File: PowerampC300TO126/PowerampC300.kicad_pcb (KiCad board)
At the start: 2 copper layers, 240 x 63 mm, 110 parts, among them J1 Conn_01x02, J2 Conn_01x02, J3 Conn_01x02, J4 Conn_01x01, J5 Conn_01x01, J6 Conn_01x01, J7 Conn_01x01, J8 Conn_01x02, J9 Conn_Coaxial, Q1 2N5551, Q10 MJE350, Q11 MJE340, Q12 MJE340, Q13 2N5551, Q14 2N5401, Q15 MJE340, Q16 MJE350, Q17 MJL3281A, Q18 MJL1302A, Q19 MJL3281A, Q2 2N5551, Q20 MJL1302A, Q21 MJL3281A, Q22 MJL1302A, Q23 MJL3281A, Q24 MJL1302A, Q3 2N5401, Q4 2N5401, Q5 2N5551, Q6 2N5551, Q7 2N5551, Q8 2N5401

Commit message: Added instructions
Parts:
- moved R24 21.3 mm to (186.4, 75.5)
- moved C5 13.8 mm to (196.5, 73.7), turned to 180 degrees
- moved R12 13.5 mm to (189.0, 69.0)
- moved C22 11.8 mm to (192.8, 69.0), turned to 0 degrees
- moved R28 11.5 mm to (182.1, 69.2)
- moved Q14 10.4 mm to (163.3, 68.8)
- moved R4 6.80 mm to (89.2, 76.0)
- moved Q4 6.50 mm to (84.8, 85.2), turned to 0 degrees
- moved C13 6.31 mm to (84.4, 68.8)
- moved R27 6.30 mm to (178.8, 72.5), turned to 0 degrees
- moved Q3 5.40 mm to (99.7, 85.0), turned to 180 degrees
- moved Q7 5.33 mm to (186.3, 85.5), turned to 180 degrees
- moved Q10 2.85 mm to (119.5, 80.4)
- moved R17 2.50 mm to (101.0, 76.0)
- moved R3 2.20 mm to (97.6, 76.0)
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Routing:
- net -48V: track 300.6 -> 283.6 mm
- net Net-(D4-Pad2): track 19.2 -> 4.69 mm
- net Net-(C22-Pad1): track 45.4 -> 56.6 mm
- net Net-(C3-Pad2): track 41.2 -> 31.4 mm
- net Net-(Q14-Pad2): track 24.5 -> 34.3 mm
- net Net-(Q12-Pad1): track 10.4 -> 19.5 mm
- net Net-(Q11-Pad3): track 15.7 -> 21.9 mm
- net Net-(Q7-Pad3): track 5.07 -> 11.2 mm
- net Net-(D3-Pad1): track 9.05 -> 2.90 mm
- net Net-(Q3-Pad1): track 4.50 -> 10.1 mm
- net Net-(C6-Pad2): track 519.5 -> 524.4 mm
- net Net-(Q7-Pad1): track 5.19 -> 10.00 mm
- net Net-(Q13-Pad2): track 15.5 -> 20.0 mm
- net Net-(Q10-Pad3): track 50.8 -> 53.6 mm
- net Net-(C9-Pad1): track 25.4 -> 27.5 mm
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
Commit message: Added option for spade terminal power connections
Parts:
- J1, J2, J3: footprint Connectors_Terminal_Blocks:TerminalBlock_bornier-2_P5.08mm -> poweramp:TerminalBlock_bornier-2_P5.08mm_with_spade
- moved J1 5.87 mm to (226.0, 98.0)
- moved C11 2.20 mm to (232.0, 91.0)
- moved R43 1.48 mm to (194.0, 103.0)
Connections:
- J2 pad 1: -48V -> GND
- J2 pad 2: GND -> -48V
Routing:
- net -48V: track 283.6 -> 296.5 mm
- net GND: track 52.5 -> 57.5 mm
- net OUTPUT: track 28.8 -> 33.0 mm
- net Net-(C11-Pad2): track 3.54 -> 5.92 mm
- net +48V: track 307.4 -> 309.7 mm
- net Net-(C6-Pad2): track 524.4 -> 525.9 mm

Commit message: Added OITPC compensation
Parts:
- added C20: NC, Capacitors_THT:C_Disc_D5.0mm_W2.5mm_P5.00mm, F.Cu at (103.3, 90.4)
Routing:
- net Net-(C20-Pad1): track 27.5 -> 30.9 mm
- net Net-(C20-Pad2): track 525.9 -> 529.2 mm
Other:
- board text added: "MODIFIED C300 AMPLIFIER BY DANIEL MARKS CC-BY-SA 4.0 V3"
- board text removed: "MODIFIED C300 AMPLIFIER BY DANIEL MARKS ORIGINAL BY MICHAEL CHUA (AMPSLAB) CC-BY-SA 4.0 V2"

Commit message: Redid star scheme again, added grounding diagram, modified drill template
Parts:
- added D11: 1N4148, Diodes_THT:D_DO-35_SOD27_P7.62mm_Horizontal, F.Cu at (195.8, 104.0)
- added D12: 1N4148, Diodes_THT:D_DO-35_SOD27_P7.62mm_Horizontal, F.Cu at (203.4, 101.4)
- added R20: 10R, Resistors_THT:R_Axial_DIN0207_L6.3mm_D2.5mm_P7.62mm_Horizontal, F.Cu at (196.0, 98.8)
- moved C6 36.6 mm to (110.6, 104.6)
- moved C23 32.4 mm to (97.3, 101.8)
- moved C3 27.1 mm to (70.0, 105.0), turned to 90 degrees
- moved C8 27.0 mm to (99.0, 88.0)
- moved C13 25.6 mm to (110.0, 69.0), turned to 0 degrees
- moved R15 25.0 mm to (104.0, 97.0)
- moved R14 24.6 mm to (107.4, 97.0)
- moved R43 23.5 mm to (216.4, 95.8), turned to 180 degrees
- moved R18 22.7 mm to (133.0, 88.0)
- moved Q8 20.9 mm to (90.3, 86.5), turned to 270 degrees
- moved R5 20.7 mm to (79.7, 95.2), turned to 270 degrees
- moved C25 19.7 mm to (133.6, 73.3), turned to 180 degrees
- moved C24 19.5 mm to (141.0, 91.0), turned to 180 degrees
- moved R3 19.4 mm to (78.2, 76.1)
- moved R17 19.3 mm to (81.8, 76.1)
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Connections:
- C2 pad 1: GND -> GNDS
- C23 pad 1: GND -> GNDS
- C24 pad 2: GND -> GNDS
- C4 pad 1: GND -> GNDS
- C8 pad 1: GND -> GNDS
- D1 pad 2: GND -> GNDS
- J8 pad 2: GND -> GNDS
- J9 pad 2: GND -> GNDS
- JP2 pad 1: GND -> GNDS
- Q8 pad 3: GND -> GNDS
- R16 pad 2: GND -> GNDS
- R2 pad 2: GND -> GNDS
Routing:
- net Net-(C20-Pad2): track 529.2 -> 489.7 mm, vias 2 -> 0
- net GNDS: track 0.00 -> 37.6 mm
- net Net-(C6-Pad1): track 48.5 -> 16.7 mm
- net Net-(Q2-Pad3): track 26.8 -> 50.9 mm
- net Net-(C20-Pad1): track 30.9 -> 53.7 mm
- net Net-(Q1-Pad3): track 29.3 -> 47.7 mm
- net Net-(C25-Pad1): track 30.0 -> 45.1 mm
- net Net-(Q10-Pad3): track 53.6 -> 66.7 mm
- net Net-(C1-Pad1): track 19.9 -> 10.5 mm
- net Net-(C10-Pad1): track 70.7 -> 61.7 mm
- net Net-(Q10-Pad1): track 14.7 -> 23.4 mm
- net Net-(C3-Pad1): track 3.72 -> 11.1 mm
- net INPUT: track 27.9 -> 21.0 mm
- net +48V: track 309.7 -> 316.0 mm
- net Net-(Q15-Pad1): track 153.6 -> 159.6 mm
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- added copper zone on F.Cu, net GNDS

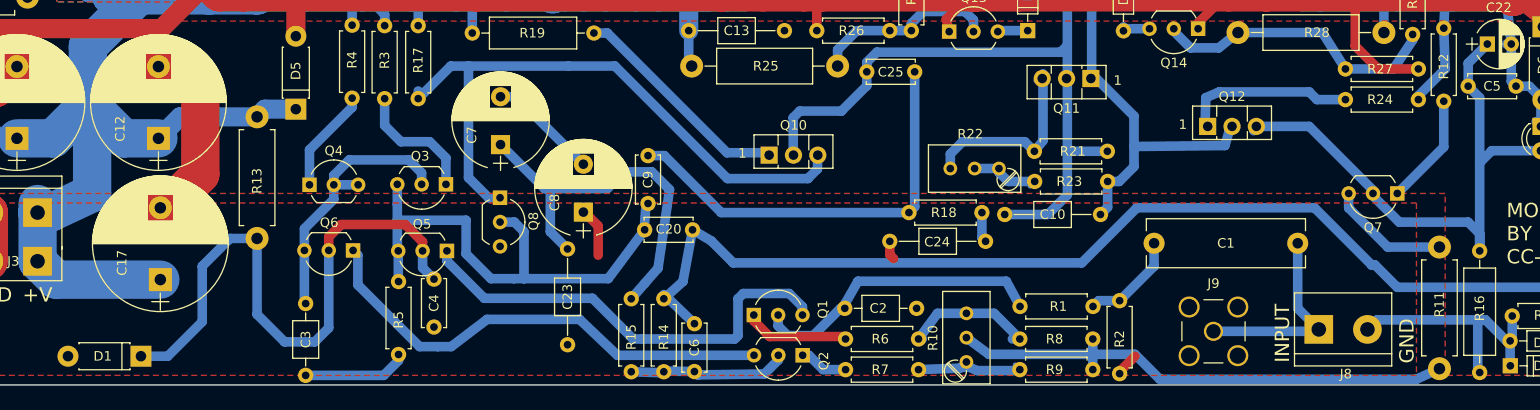
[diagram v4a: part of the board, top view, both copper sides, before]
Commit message: Changed components for lower quiescent power
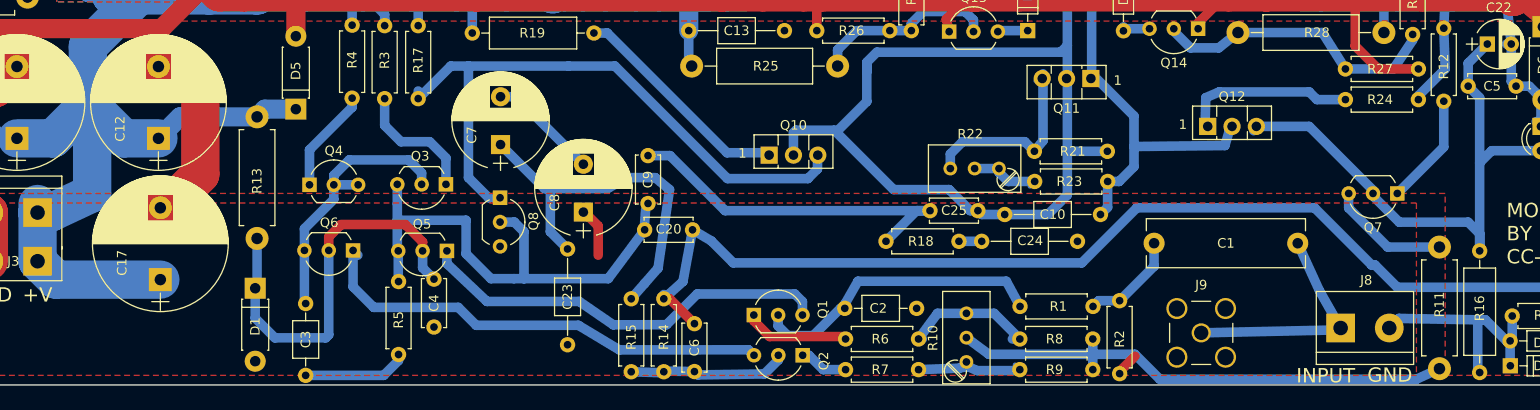
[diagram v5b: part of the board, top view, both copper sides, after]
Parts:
- moved C25 14.6 mm to (135.2, 87.8), turned to 0 degrees
- moved D1 13.9 mm to (64.7, 95.9), turned to 270 degrees
- moved R18 3.84 mm to (130.6, 91.0)
- moved J8 2.28 mm to (178.1, 100.0)
- moved J9 1.29 mm to (163.5, 100.6)
- moved C24 0.40 mm to (140.6, 91.0), turned to 0 degrees
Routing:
- net Net-(C10-Pad2): track 90.4 -> 112.3 mm
- net Net-(C4-Pad2): track 62.9 -> 42.9 mm
- net Net-(C25-Pad1): track 45.1 -> 37.8 mm
- net GNDS: track 37.6 -> 33.4 mm
- net INPUT: track 21.0 -> 24.6 mm
- net Net-(Q1-Pad3): track 47.7 -> 44.4 mm
- net Net-(Q2-Pad3): track 50.9 -> 50.0 mm
- net Net-(C24-Pad1): track 3.16 -> 2.38 mm
- net Net-(C23-Pad2): track 40.6 -> 39.9 mm
- net Net-(C20-Pad2): track 489.7 -> 490.3 mm

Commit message: Added base stopper resistors
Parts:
- added C21: 10 uF, Capacitors_THT:C_Disc_D5.0mm_W2.5mm_P5.00mm, F.Cu at (153.5, 87.8)
- added R44: 2R2, Resistors_THT:R_Axial_DIN0411_L9.9mm_D3.6mm_P15.24mm_Horizontal, F.Cu at (130.3, 55.5)
- added R45: 2R2, Resistors_THT:R_Axial_DIN0411_L9.9mm_D3.6mm_P15.24mm_Horizontal, F.Cu at (107.3, 55.4)
- added R46: 2R2, Resistors_THT:R_Axial_DIN0411_L9.9mm_D3.6mm_P15.24mm_Horizontal, F.Cu at (80.2, 55.2)
- added R47: 2R2, Resistors_THT:R_Axial_DIN0411_L9.9mm_D3.6mm_P15.24mm_Horizontal, F.Cu at (55.2, 55.3)
- added R48: 2R2, Resistors_THT:R_Axial_DIN0411_L9.9mm_D3.6mm_P15.24mm_Horizontal, F.Cu at (226.7, 55.0)
- added R49: 2R2, Resistors_THT:R_Axial_DIN0411_L9.9mm_D3.6mm_P15.24mm_Horizontal, F.Cu at (201.7, 55.0)
- added R50: 2R2, Resistors_THT:R_Axial_DIN0411_L9.9mm_D3.6mm_P15.24mm_Horizontal, F.Cu at (176.8, 55.2)
- added R51: 2R2, Resistors_THT:R_Axial_DIN0411_L9.9mm_D3.6mm_P15.24mm_Horizontal, F.Cu at (151.8, 55.3)
- Q10, Q11, Q12, Q15, Q16: footprint TO_SOT_Packages_THT:TO-126_Vertical -> TO_SOT_Packages_THT:TO-220-3_Vertical
- R24: value 56R -> 120R
- R25, R28: value 3k3 -> 6k8
- moved C10 29.2 mm to (153.2, 59.0)
- moved Q17 2.80 mm to (40.0, 47.2)
- moved Q18 2.80 mm to (242.0, 47.2)
- moved Q19 2.80 mm to (65.0, 47.2)
- moved Q20 2.80 mm to (217.0, 47.2)
- moved Q21 2.80 mm to (90.0, 47.2)
- moved Q22 2.80 mm to (192.0, 47.2)
- moved Q23 2.80 mm to (115.0, 47.2)
- moved Q24 2.80 mm to (167.0, 47.2)
- moved C25 1.81 mm to (133.4, 88.0)
- moved R39 1.71 mm to (109.2, 60.7)
- moved R35 1.70 mm to (55.0, 60.7)
- moved R37 1.67 mm to (82.2, 60.6)
- moved R33 1.65 mm to (27.7, 60.6)
- moved Q7 1.60 mm to (185.6, 86.0)
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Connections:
- Q17 pad 1: Net-(Q15-Pad1) -> Net-(Q17-Pad1)
- Q18 pad 1: Net-(Q16-Pad1) -> Net-(Q18-Pad1)
- Q19 pad 1: Net-(Q15-Pad1) -> Net-(Q19-Pad1)
- Q20 pad 1: Net-(Q16-Pad1) -> Net-(Q20-Pad1)
- Q21 pad 1: Net-(Q15-Pad1) -> Net-(Q21-Pad1)
- Q22 pad 1: Net-(Q16-Pad1) -> Net-(Q22-Pad1)
- Q23 pad 1: Net-(Q15-Pad1) -> Net-(Q23-Pad1)
- Q24 pad 1: Net-(Q16-Pad1) -> Net-(Q24-Pad1)
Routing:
- net Net-(Q15-Pad1): track 159.6 -> 124.4 mm
- net Net-(C10-Pad2): track 112.3 -> 83.9 mm
- net Net-(Q16-Pad1): track 165.2 -> 142.8 mm
- net +48V: track 316.0 -> 334.8 mm
- net Net-(C10-Pad1): track 61.7 -> 78.8 mm
- net Net-(Q19-Pad1): track 0.00 -> 13.6 mm
- net Net-(Q21-Pad1): track 0.00 -> 12.2 mm
- net Net-(Q17-Pad1): track 0.00 -> 11.9 mm
- net Net-(Q23-Pad1): track 0.00 -> 10.9 mm
- net Net-(Q24-Pad1): track 0.00 -> 10.7 mm
- net Net-(Q22-Pad1): track 0.00 -> 10.6 mm
- net Net-(Q20-Pad1): track 0.00 -> 10.4 mm
- net Net-(Q18-Pad1): track 0.00 -> 10.3 mm
- net GNDS: track 33.4 -> 27.8 mm
- net -48V: track 298.3 -> 303.1 mm
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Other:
- board text added: "MODIFIED C300 AMPLIFIER BY DANIEL MARKS CC-BY-SA 4.0 V4"
- board text removed: "MODIFIED C300 AMPLIFIER BY DANIEL MARKS CC-BY-SA 4.0 V3"

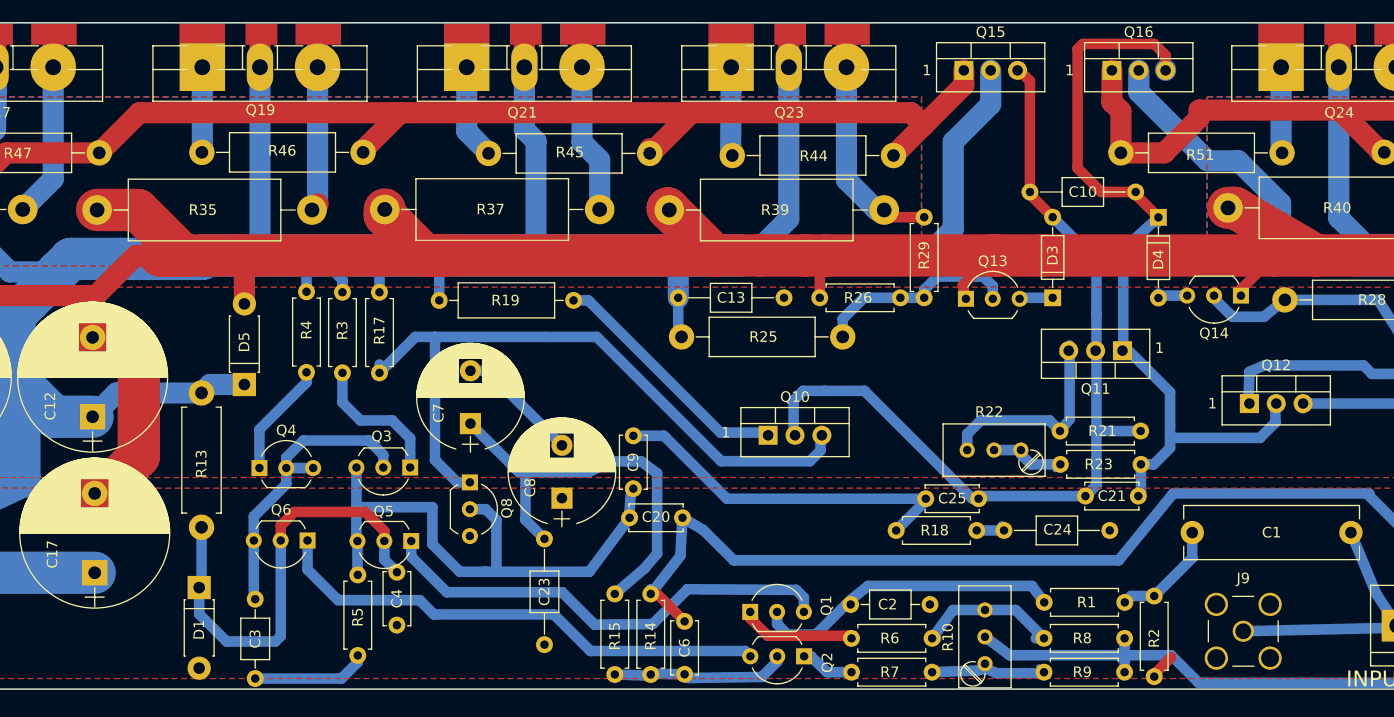
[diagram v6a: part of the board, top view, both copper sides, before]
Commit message: Additions of optional zener diodes to limit current surges
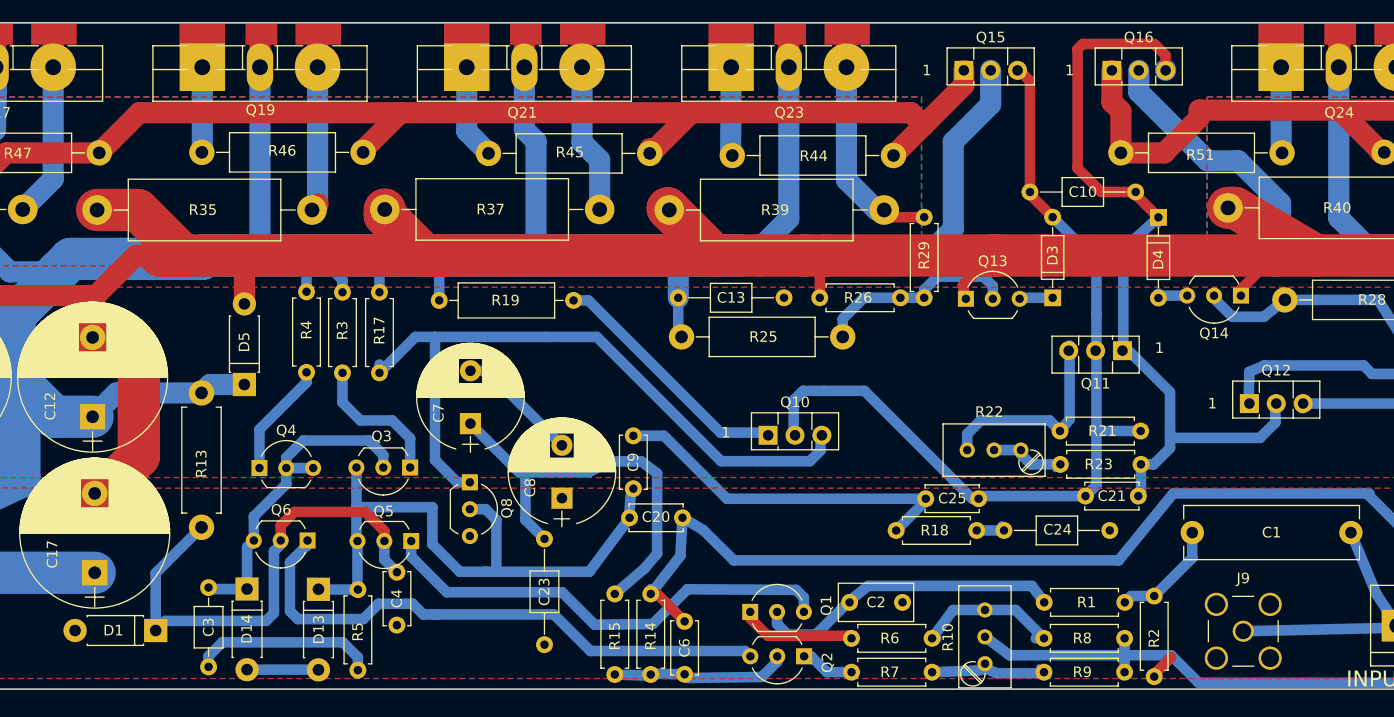
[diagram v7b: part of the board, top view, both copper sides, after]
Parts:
- added D13: NC, Diodes_THT:D_DO-41_SOD81_P7.62mm_Horizontal, F.Cu at (76.0, 96.6)
- added D14: NC, Diodes_THT:D_DO-41_SOD81_P7.62mm_Horizontal, F.Cu at (69.2, 96.5)
- C2: footprint Capacitors_THT:C_Axial_L3.8mm_D2.6mm_P7.50mm_Horizontal -> Capacitors_THT:C_Rect_L7.0mm_W3.5mm_P5.00mm
- Q10, Q11, Q12, Q15, Q16: footprint TO_SOT_Packages_THT:TO-220-3_Vertical -> TO_SOT_Packages_THT:TO-126_Vertical
- moved D1 5.78 mm to (60.6, 100.5), turned to 180 degrees
- moved C3 4.55 mm to (65.6, 103.9)
- moved C2 2.61 mm to (131.2, 97.8)
- moved R5 1.39 mm to (79.7, 96.6)
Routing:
- net Net-(D13-Pad2): track 0.00 -> 6.76 mm
- net Net-(Q2-Pad3): track 48.8 -> 55.4 mm
- net Net-(C3-Pad1): track 11.1 -> 17.5 mm
- net Net-(C20-Pad1): track 53.7 -> 58.9 mm
- net Net-(C4-Pad2): track 43.3 -> 47.5 mm
- net Net-(C3-Pad2): track 28.8 -> 31.8 mm

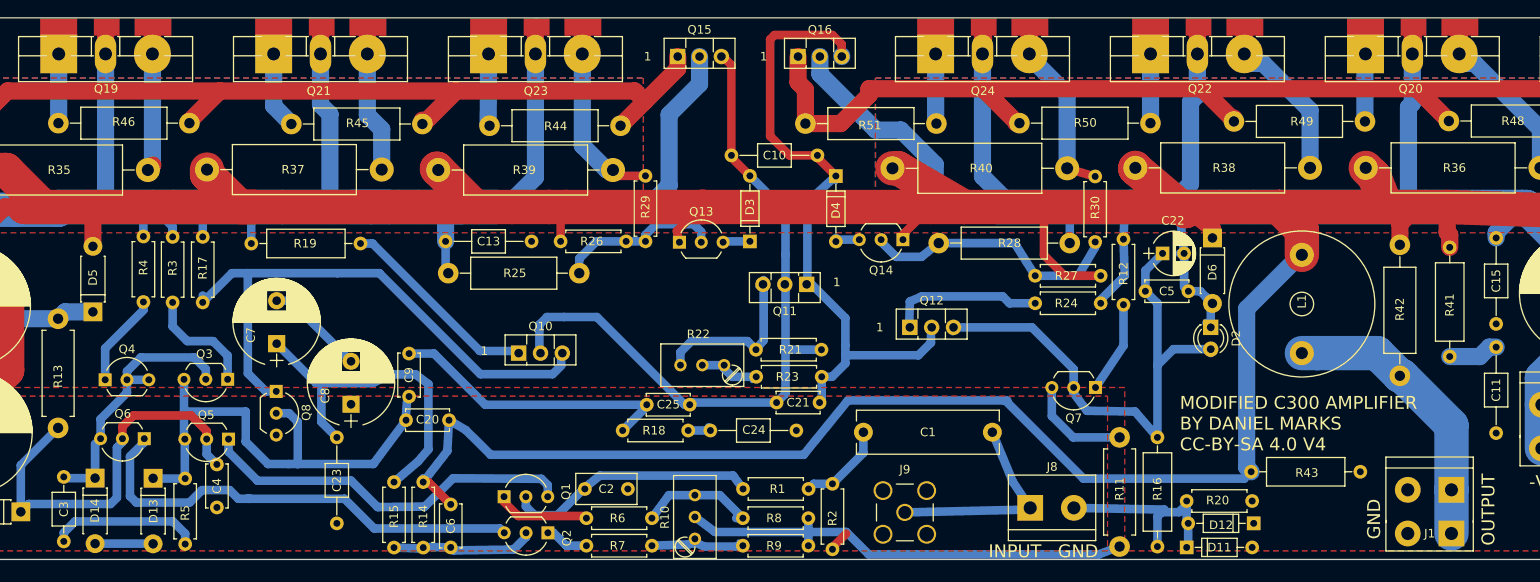
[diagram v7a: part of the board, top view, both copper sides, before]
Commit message: Changed to use optotriac shutoff of bias
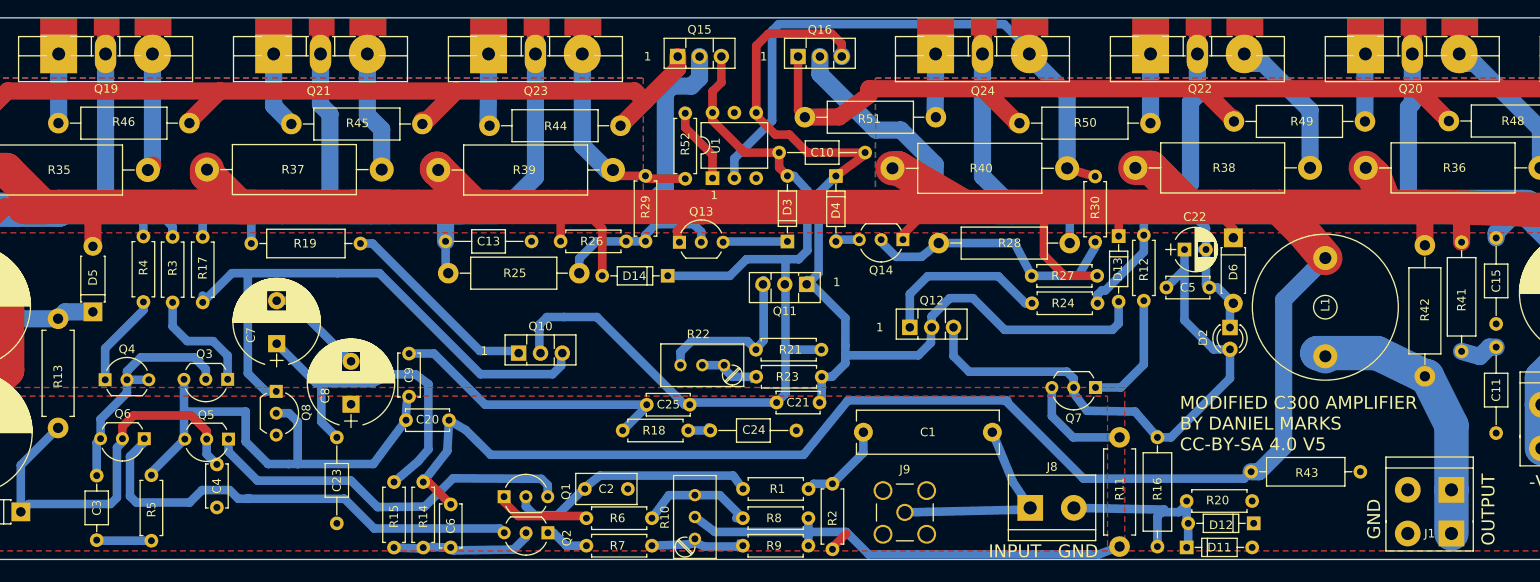
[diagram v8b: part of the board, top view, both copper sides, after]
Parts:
- added R52: 100R, Resistors_THT:R_Axial_DIN0207_L6.3mm_D2.5mm_P7.62mm_Horizontal, F.Cu at (137.9, 54.1)
- added U1: MOC3020M, Housings_DIP:DIP-6_W7.62mm, F.Cu at (141.1, 61.6)
- D13, D14: value NC -> 1N4148; footprint Diodes_THT:D_DO-41_SOD81_P7.62mm_Horizontal -> Diodes_THT:D_DO-35_SOD27_P7.62mm_Horizontal
- moved D13 115.8 mm to (188.3, 68.4)
- moved D14 70.6 mm to (135.8, 73.0), turned to 180 degrees
- moved C10 5.56 mm to (158.8, 58.7)
- moved D3 4.36 mm to (149.8, 69.0)
- moved R5 3.95 mm to (75.8, 96.2)
- moved C3 3.83 mm to (69.4, 103.8)
- moved R42 2.91 mm to (223.9, 69.5)
- moved L1 2.75 mm to (212.3, 82.4)
- moved C22 2.59 mm to (195.9, 70.0)
- moved C5 2.48 mm to (198.8, 74.4)
- moved D6 2.43 mm to (201.6, 68.6)
- moved R12 2.42 mm to (191.2, 68.3)
- moved D2 2.24 mm to (201.2, 79.0)
- moved R41 1.50 mm to (228.2, 81.8)
- moved R51 0.74 mm to (151.8, 54.6)
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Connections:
- C10 pad 1: Net-(C10-Pad1) -> BIAS2
- C10 pad 2: Net-(C10-Pad2) -> BIAS1
- C21 pad 1: Net-(C10-Pad1) -> BIAS2
- C21 pad 2: Net-(C10-Pad2) -> BIAS1
- C25 pad 2: Net-(C10-Pad2) -> BIAS1
- D13 pad 1: Net-(C20-Pad1) -> Net-(C20-Pad2)
- D13 pad 2: Net-(D13-Pad2) -> BIAS2
- D14 pad 1: Net-(C3-Pad2) -> BIAS1
- D14 pad 2: Net-(D13-Pad2) -> Net-(C20-Pad2)
- D3 pad 2: Net-(C10-Pad2) -> BIAS1
- D4 pad 1: Net-(C10-Pad1) -> BIAS2
- Q10 pad 2: Net-(C10-Pad2) -> BIAS1
- Q11 pad 1: Net-(C10-Pad1) -> BIAS2
- Q11 pad 2: Net-(C10-Pad2) -> BIAS1
- Q12 pad 2: Net-(C10-Pad1) -> BIAS2
- Q15 pad 3: Net-(C10-Pad2) -> BIAS1
- Q16 pad 3: Net-(C10-Pad1) -> BIAS2
- R21 pad 2: Net-(C10-Pad2) -> BIAS1
- R23 pad 1: Net-(C10-Pad1) -> BIAS2
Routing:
- net BIAS2: track 0.00 -> 115.7 mm
- net BIAS1: track 0.00 -> 105.6 mm
- net Net-(C10-Pad2): track 83.9 -> 0.00 mm
- net Net-(C10-Pad1): track 78.8 -> 0.00 mm
- net Net-(Q24-Pad3): track 21.8 -> 72.7 mm
- net Net-(C20-Pad2): track 489.6 -> 503.1 mm
- net Net-(C3-Pad1): track 17.5 -> 6.39 mm
- net Net-(R52-Pad1): track 0.00 -> 8.86 mm
- net Net-(D13-Pad2): track 6.76 -> 0.00 mm
- net Net-(Q23-Pad3): track 23.0 -> 27.7 mm
- net Net-(D3-Pad1): track 3.16 -> 7.66 mm
- net Net-(C22-Pad1): track 62.8 -> 67.0 mm
- net Net-(C3-Pad2): track 31.8 -> 27.7 mm
- net Net-(Q7-Pad1): track 10.6 -> 14.2 mm
- net Net-(C20-Pad1): track 58.9 -> 56.3 mm
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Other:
- board text added: "MODIFIED C300 AMPLIFIER BY DANIEL MARKS CC-BY-SA 4.0 V5"
- board text removed: "MODIFIED C300 AMPLIFIER BY DANIEL MARKS CC-BY-SA 4.0 V4"
